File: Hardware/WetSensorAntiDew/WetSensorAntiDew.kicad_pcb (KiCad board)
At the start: 2 copper layers, 14 parts, among them J1 Teensy Connector, J2 Connector to BME280, J3 1-4 to HeatedWetSensor | 5-7 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, J4 Teensy Connector, J5 Connector to power supply, Q1 MOSFET N-CH, U1 AMS1117

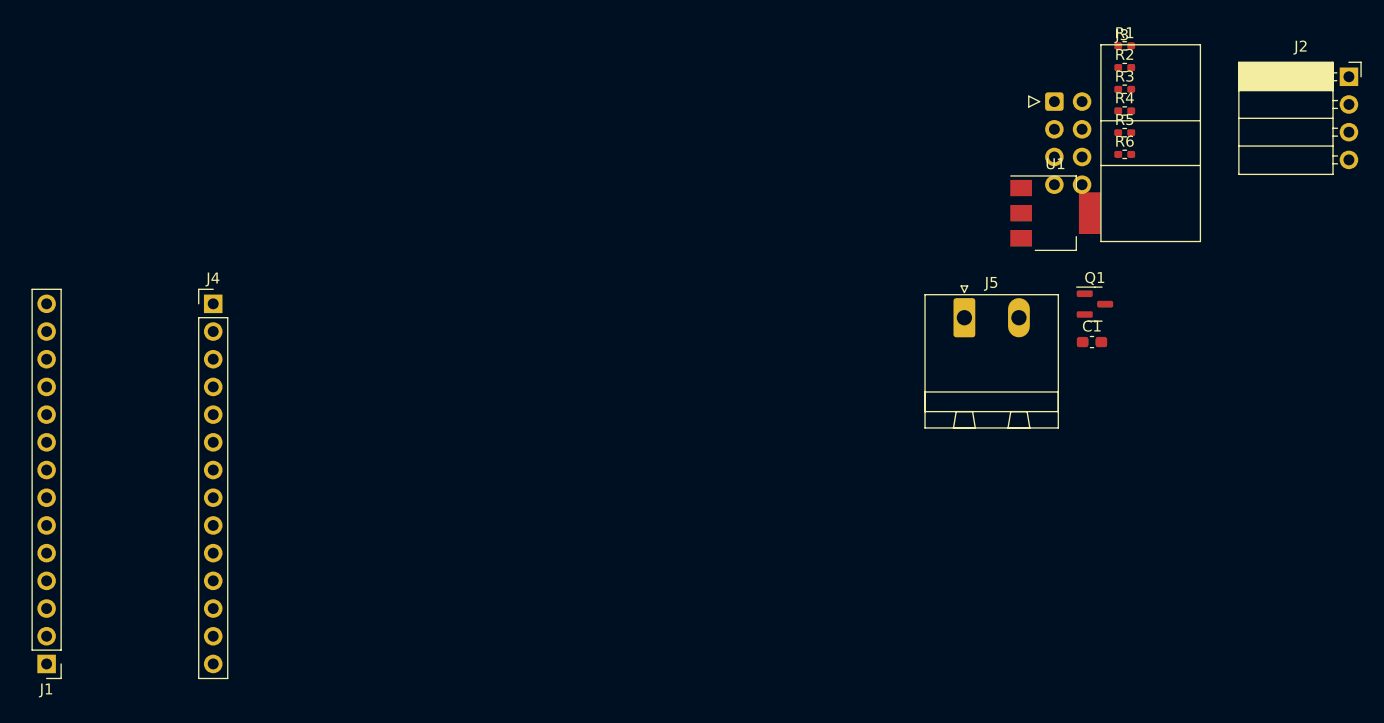
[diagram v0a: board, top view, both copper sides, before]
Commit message: finished Pcb layout
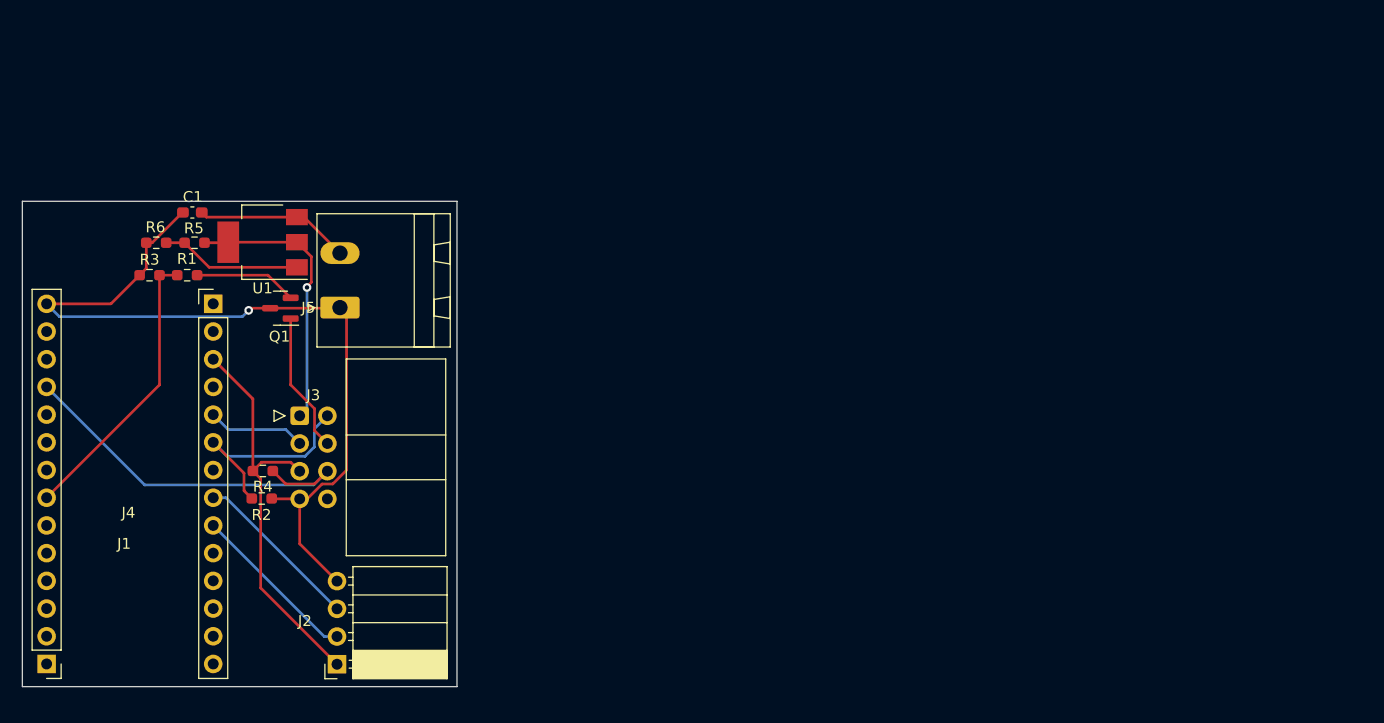
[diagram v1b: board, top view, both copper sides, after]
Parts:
- R1, R2, R3, R4, R5, R6: footprint Resistor_SMD:R_0402_1005Metric_Pad0.72x0.64mm_HandSolder -> Resistor_SMD:R_0603_1608Metric_Pad0.98x0.95mm_HandSolder
- moved J2 107.3 mm to (148.0, 104.6), turned to 180 degrees
- moved R3 91.0 mm to (130.8, 69.0)
- moved R6 89.2 mm to (131.4, 66.0)
- moved R1 88.5 mm to (134.3, 69.0), turned to 180 degrees
- moved R2 88.4 mm to (141.1, 89.5), turned to 180 degrees
- moved R5 85.9 mm to (135.0, 66.0)
- moved R4 85.6 mm to (141.2, 86.9), turned to 180 degrees
- moved C1 83.3 mm to (134.8, 63.2), turned to 180 degrees
- moved J3 75.0 mm to (144.6, 81.9)
- moved Q1 74.7 mm to (142.8, 72.0), turned to 180 degrees
- moved U1 72.7 mm to (141.2, 66.0), turned to 180 degrees
- moved J5 57.3 mm to (148.3, 72.0), turned to 90 degrees
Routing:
- net Earth: track 0.00 -> 77.2 mm, vias 0 -> 1
- net +3V3: track 0.00 -> 37.6 mm
- net PIN2: track 0.00 -> 36.0 mm
- net PIN6: track 0.00 -> 26.3 mm
- net +12V: track 0.00 -> 25.6 mm, vias 0 -> 1
- net DRIVE: track 0.00 -> 20.1 mm
- net SDA: track 0.00 -> 15.6 mm
- net SCL: track 0.00 -> 15.6 mm
- net Net-(J5-Pin_2): track 0.00 -> 14.2 mm
- net Net-(U1-ADJ): track 0.00 -> 12.9 mm
- net MOSFET: track 0.00 -> 12.8 mm
- net Net-(Q1-S): track 0.00 -> 9.43 mm
- net SENSE: track 0.00 -> 9.02 mm
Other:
- board outline added: 39.9 x 44.5 mm

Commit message: WIP new voltage regulator
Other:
- board size 39.9 x 44.5 mm -> 32.3 x 44.5 mm
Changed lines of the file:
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@@
     )
   )
-  (gr_rect (start 119.175 62.2) (end 159.025 106.7)
+  (gr_rect (start 119.175 62.2) (end 151.45 106.7)
     (stroke (width 0.1) (type default)) (fill none) (layer "Edge.Cuts"))
   (dimension (type aligned) (layer "User.1")

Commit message: Updates to board
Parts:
- removed R2: R, Resistor_SMD:R_0603_1608Metric_Pad0.98x0.95mm_HandSolder
- added C2: C, Capacitor_SMD:C_0603_1608Metric_Pad1.08x0.95mm_HandSolder, F.Cu at (369.7, 64.6)
- added C3: C, Capacitor_SMD:C_0603_1608Metric_Pad1.08x0.95mm_HandSolder, F.Cu at (369.7, 67.2)
- added C5: C, Capacitor_SMD:C_0603_1608Metric_Pad1.08x0.95mm_HandSolder, F.Cu at (369.7, 69.7)
- added J8: 6P6C, Connector_RJ:RJ12_Amphenol_54601, F.Cu at (347.4, 120.7)
- added JP1: SolderJumper_3_Bridged12, Jumper:SolderJumper-3_P1.3mm_Bridged12_Pad1.0x1.5mm_NumberLabels, F.Cu at (370.3, 77.7)
- added R10: 10k, Resistor_SMD:R_0603_1608Metric_Pad0.98x0.95mm_HandSolder, F.Cu at (374.0, 69.7)
- added R11: 100K, Resistor_SMD:R_0603_1608Metric_Pad0.98x0.95mm_HandSolder, F.Cu at (374.0, 72.2)
- added U3: STM32F103C6Tx, Package_QFP:LQFP-48_7x7mm_P0.5mm, F.Cu at (365.8, 109.2)
- J2: moved to B.Cu
- J3: value 1-4 to HeatedWetSensor | 5-7 to TempSensor -> 4P4C; footprint Connector_IDC:IDC-Header_2x04_P2.54mm_Horizontal -> footprints:BEL_SS-6444-NF
- moved R6 242.6 mm to (374.0, 67.2)
- moved J3 239.4 mm to (379.7, 127.0)
- moved R5 239.1 mm to (374.0, 64.6)
- moved R3 238.9 mm to (369.7, 74.7)
- moved R1 235.4 mm to (369.7, 72.2), turned to 0 degrees
- moved C1 234.9 mm to (369.7, 62.1), turned to 0 degrees
- moved R4 234.1 mm to (374.0, 62.1), turned to 0 degrees
- moved Q1 232.8 mm to (375.6, 78.2), turned to 0 degrees
- moved J2 227.9 mm to (375.9, 106.7)
- moved J1 227.5 mm to (345.1, 63.2), turned to 0 degrees
- moved J5 222.0 mm to (363.3, 127.3), turned to 0 degrees
- moved U1 218.4 mm to (357.0, 99.5), turned to 0 degrees
- moved J4 213.2 mm to (349.7, 63.2)
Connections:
- C1 pad 1: Net-(J5-Pin_2) -> +12V
- J1 pad 7: PIN6 -> unconnected-(J1-Pin_7-Pad7)
- J3 pad 1: +12V -> unconnected-(J3-Pad1)
- J3 pad 2: DRIVE -> unconnected-(J3-Pad2)
- J3 pad 3: SENSE -> unconnected-(J3-Pad3)
- J3 pad 4: MOSFET -> unconnected-(J3-Pad4)
- J5 pad 2: Net-(J5-Pin_2) -> +12V
- Q1 pad 1: MOSFET -> Net-(Q1-G)
- Q1 pad 2: Net-(Q1-S) -> Earth
- Q1 pad 3: Earth -> MOSFET
- R1 pad 1: Net-(Q1-S) -> Net-(Q1-G)
- R5 pad 2: +12V -> +3V3
- U1 pad 2: +12V -> +3V3
- U1 pad 3: Net-(J5-Pin_2) -> +12V
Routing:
- net Earth: track 77.2 -> 6.71 mm, vias 1 -> 4
- net PIN2: track 36.0 -> 0.00 mm
- net PIN6: track 26.3 -> 0.00 mm
- net +12V: track 25.6 -> 0.00 mm, vias 1 -> 0
- net DRIVE: track 20.1 -> 0.00 mm
- net Net-(J5-Pin_2): track 14.2 -> 0.00 mm
- net Net-(U1-ADJ): track 12.9 -> 0.00 mm
- net MOSFET: track 12.8 -> 0.00 mm
- net SDA: track 15.6 -> 6.10 mm
- net Net-(Q1-S): track 9.43 -> 0.00 mm
- net SENSE: track 9.02 -> 0.00 mm
- net SCL: track 15.6 -> 6.95 mm
- net +3V3: track 37.6 -> 29.6 mm
- added copper zone on B.Cu, net Earth
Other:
- board size 32.3 x 44.5 mm -> 96.5 x 104.1 mm

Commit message: More progress
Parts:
- removed J1, J4: Teensy Connector, Connector_PinHeader_2.54mm:PinHeader_1x14_P2.54mm_Vertical
- added C4: C, Capacitor_SMD:C_0603_1608Metric_Pad1.08x0.95mm_HandSolder, F.Cu at (136.0, 88.2)
- added C6: C, Capacitor_SMD:C_0603_1608Metric_Pad1.08x0.95mm_HandSolder, F.Cu at (136.0, 90.7)
- added D1: D_Schottky, Diode_SMD:D_SOD-323, F.Cu at (163.4, 103.4)
- added J6: Conn_01x04_Socket, Connector:FanPinHeader_1x04_P2.54mm_Vertical, F.Cu at (101.4, 95.8)
- added JP2: SolderJumper_2_Open, Jumper:SolderJumper-2_P1.3mm_Open_Pad1.0x1.5mm, F.Cu at (140.4, 88.7)
- added JP3: SolderJumper_2_Open, Jumper:SolderJumper-2_P1.3mm_Open_Pad1.0x1.5mm, F.Cu at (145.3, 93.3)
- added R2: R, Resistor_SMD:R_0603_1608Metric_Pad0.98x0.95mm_HandSolder, F.Cu at (136.0, 93.2)
- added R7: 10k, Resistor_SMD:R_0603_1608Metric_Pad0.98x0.95mm_HandSolder, F.Cu at (163.4, 100.6)
- added SW1: SW_Push, footprints:228EJVAYFR, F.Cu at (156.4, 104.3)
- added U2: ~, Package_DFN_QFN:DFN-12-1EP_3x3mm_P0.5mm_EP1.6x2.5mm_ThermalVias, F.Cu at (159.5, 110.7)
- added Y1: Crystal_GND24_Small, Crystal:Crystal_SMD_3225-4Pin_3.2x2.5mm, F.Cu at (154.3, 110.7)
- moved U1 271.4 mm to (86.2, 81.7)
- moved Q1 267.2 mm to (108.9, 95.0)
- moved J2 252.3 mm to (123.7, 104.0)
- moved J3 252.3 mm to (127.5, 124.3)
- moved J8 252.3 mm to (95.1, 118.0)
- moved C1 252.3 mm to (117.4, 59.4)
- moved C2 252.3 mm to (117.4, 62.0)
- moved C3 252.3 mm to (117.4, 64.5)
- moved C5 252.3 mm to (117.4, 67.0)
- moved J5 252.3 mm to (111.0, 124.6)
- moved JP1 252.3 mm to (118.1, 75.0)
- moved R1 252.3 mm to (117.4, 69.5)
- moved R10 252.3 mm to (121.8, 67.0)
- moved R11 252.3 mm to (121.8, 69.5)
- moved R3 252.3 mm to (117.4, 72.0)
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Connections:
- net Net-(U3-BOOT0) renamed /Boot
- J2 pad 4: Earth -> unconnected-(J2-Pin_4-Pad4)
- J3 pad 3: unconnected-(J3-Pad3) -> WET2
- J3 pad 4: unconnected-(J3-Pad4) -> WET1
- J8 pad 4: DRIVE -> WET2
- J8 pad 5: SENSE -> WET1
- U3 pad 10: unconnected-(U3-PA0-Pad10) -> PA0
- U3 pad 5: unconnected-(U3-PD0-Pad5) -> OSCIN
- U3 pad 6: unconnected-(U3-PD1-Pad6) -> OSCOUT
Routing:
- net +3V3: track 29.6 -> 0.30 mm
- net SCL: track 6.95 -> 0.00 mm
- net Earth: track 6.71 -> 0.00 mm, vias 4 -> 0
- net SDA: track 6.10 -> 0.35 mm
- removed copper zone on B.Cu, net Earth

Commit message: finished pcb layout
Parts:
- removed JP1: SolderJumper_3_Bridged12, Jumper:SolderJumper-3_P1.3mm_Bridged12_Pad1.0x1.5mm_NumberLabels
- added C7: C, Capacitor_SMD:C_0603_1608Metric_Pad1.08x0.95mm_HandSolder, F.Cu at (108.2, 115.1)
- J2: footprint Connector_PinSocket_2.54mm:PinSocket_1x04_P2.54mm_Horizontal -> Connector_PinSocket_2.54mm:PinSocket_1x05_P2.54mm_Horizontal; moved to F.Cu
- J5: footprint Connector_Phoenix_MSTB:PhoenixContact_MSTBA_2,5_2-G_1x02_P5.00mm_Horizontal -> Connector_Phoenix_MC:PhoenixContact_MC_1,5_2-G-3.81_1x02_P3.81mm_Horizontal
- R7: value 10k -> 1.5k
- moved D1 63.5 mm to (100.3, 110.7), turned to 90 degrees
- moved R7 58.9 mm to (104.6, 103.7), turned to -90 degrees
- moved R4 56.5 mm to (117.2, 115.7), turned to 90 degrees
- moved U2 56.1 mm to (103.5, 111.4), turned to 180 degrees
- moved JP3 55.0 mm to (94.5, 114.2), turned to 90 degrees
- moved C1 52.6 mm to (106.5, 110.9), turned to 90 degrees
- moved C2 52.2 mm to (98.6, 110.6), turned to 90 degrees
- moved R5 51.1 mm to (110.7, 111.9)
- moved C3 50.3 mm to (115.7, 114.8), turned to 90 degrees
- moved R6 48.4 mm to (108.2, 110.9), turned to -90 degrees
- moved SW1 47.9 mm to (110.3, 91.2), turned to -90 degrees
- moved R1 46.0 mm to (96.7, 110.6), turned to 90 degrees
- moved U1 45.4 mm to (112.8, 118.5), turned to 90 degrees
- moved JP2 44.4 mm to (104.3, 114.6), turned to 180 degrees
- moved R3 41.2 mm to (97.6, 108.2), turned to 180 degrees
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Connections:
- R11 pad 2: Net-(JP1-C) -> Earth
- U2 pad 13: (no net) -> Earth
- U2 pad 6: unconnected-(U2-CLMODE-Pad6) -> Earth
- U3 pad 10: PA0 -> unconnected-(U3-PA0-Pad10)
- U3 pad 29: unconnected-(U3-PA8-Pad29) -> PA0
- U3 pad 31: unconnected-(U3-PA10-Pad31) -> PIN6
- U3 pad 32: unconnected-(U3-PA11-Pad32) -> PB5
- U3 pad 41: FWD -> unconnected-(U3-PB5-Pad41)
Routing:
- net Earth: track 0.00 -> 87.3 mm, vias 0 -> 2
- net +3V3: track 0.30 -> 70.0 mm, vias 0 -> 5
- net PIN2: track 0.00 -> 34.7 mm
- net +12V: track 0.00 -> 33.8 mm
- net PIN6: track 0.00 -> 32.1 mm
- net WET1: track 0.00 -> 29.4 mm
- net WET2: track 0.00 -> 26.0 mm
- net /SWIO: track 0.00 -> 24.9 mm, vias 0 -> 1
- net /SWCLK: track 0.00 -> 20.3 mm, vias 0 -> 1
- net PB5: track 0.00 -> 19.5 mm
- net Net-(U3-NRST): track 0.00 -> 14.9 mm
- net MOSFET: track 0.00 -> 13.6 mm, vias 0 -> 1
- net Net-(U1-ADJ): track 0.00 -> 12.9 mm
- net PA0: track 0.00 -> 12.3 mm, vias 0 -> 2
- net +12C: track 0.00 -> 12.2 mm
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- added copper zone on B.Cu, net Earth
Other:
- board size 96.5 x 104.1 mm -> 37.5 x 48.6 mm

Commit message: Final* PCB design
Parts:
- moved C7 1.12 mm to (108.3, 116.2)
- renumbered JP2 to JPload, JP3 to JPmos
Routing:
- net +3V3: track 70.0 -> 69.5 mm
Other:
- board size 37.5 x 48.6 mm -> 38.1 x 48.8 mm
